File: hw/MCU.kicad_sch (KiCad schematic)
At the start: 18 parts, among them J2 Conn_01x06, SW2 SKRPACE010, SW3 SKRPACE010, U2 N32L406RBL7, Y2 XL2EL89COI-111YLC-8M

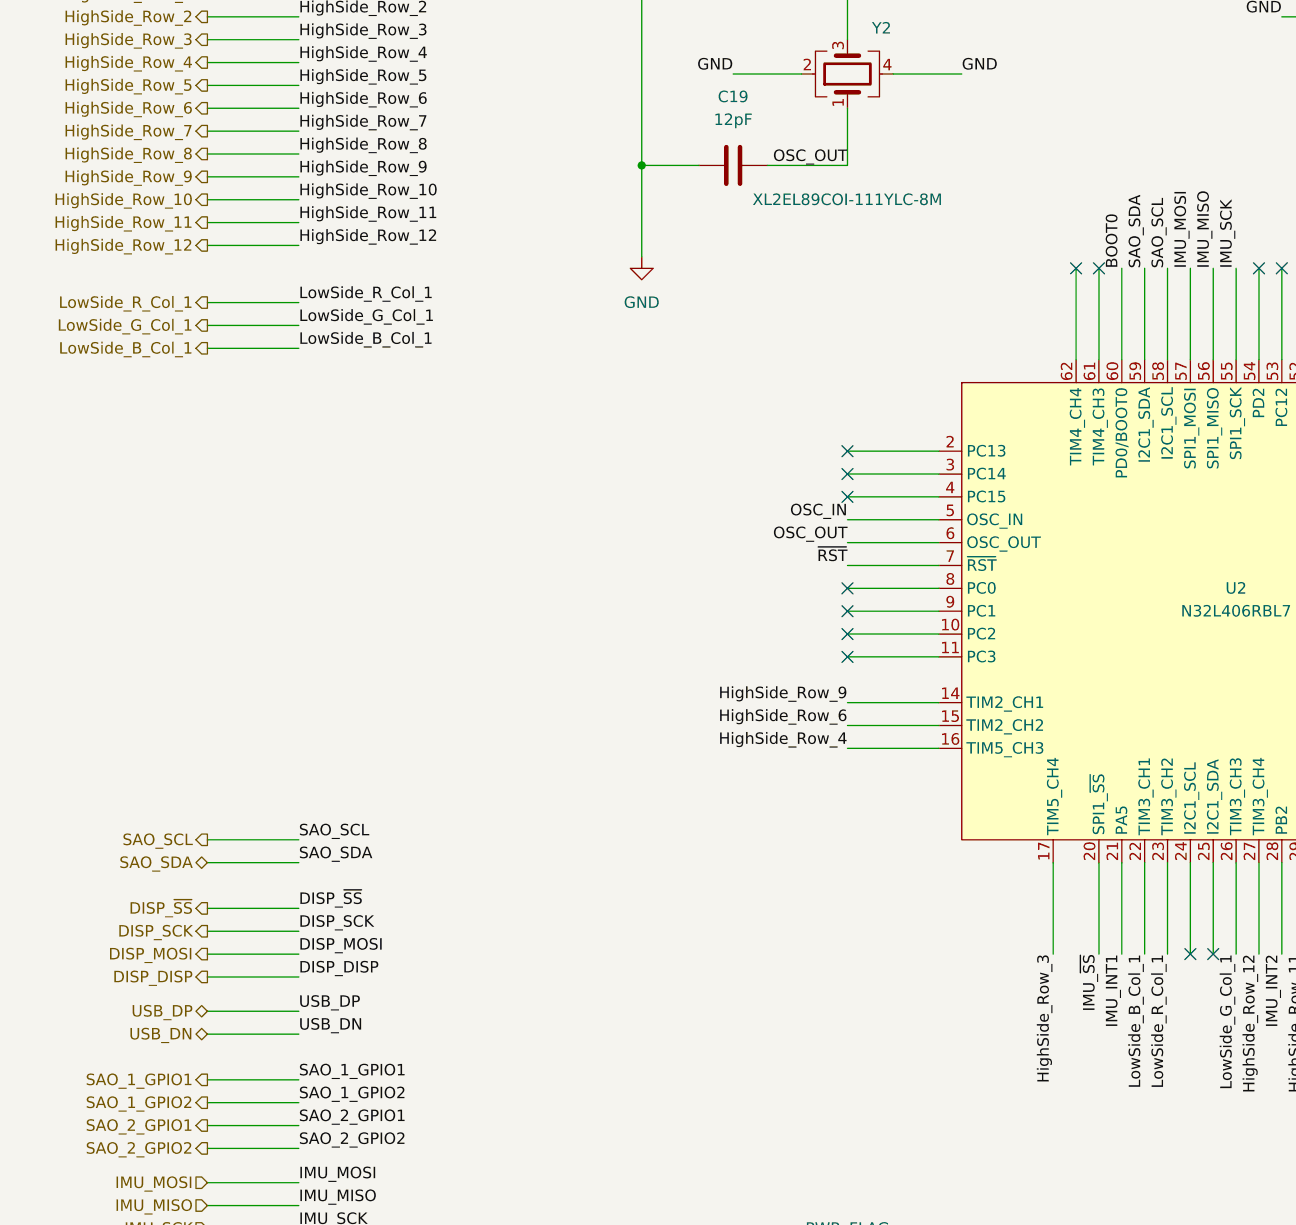
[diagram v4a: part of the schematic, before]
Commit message: added a UART connector
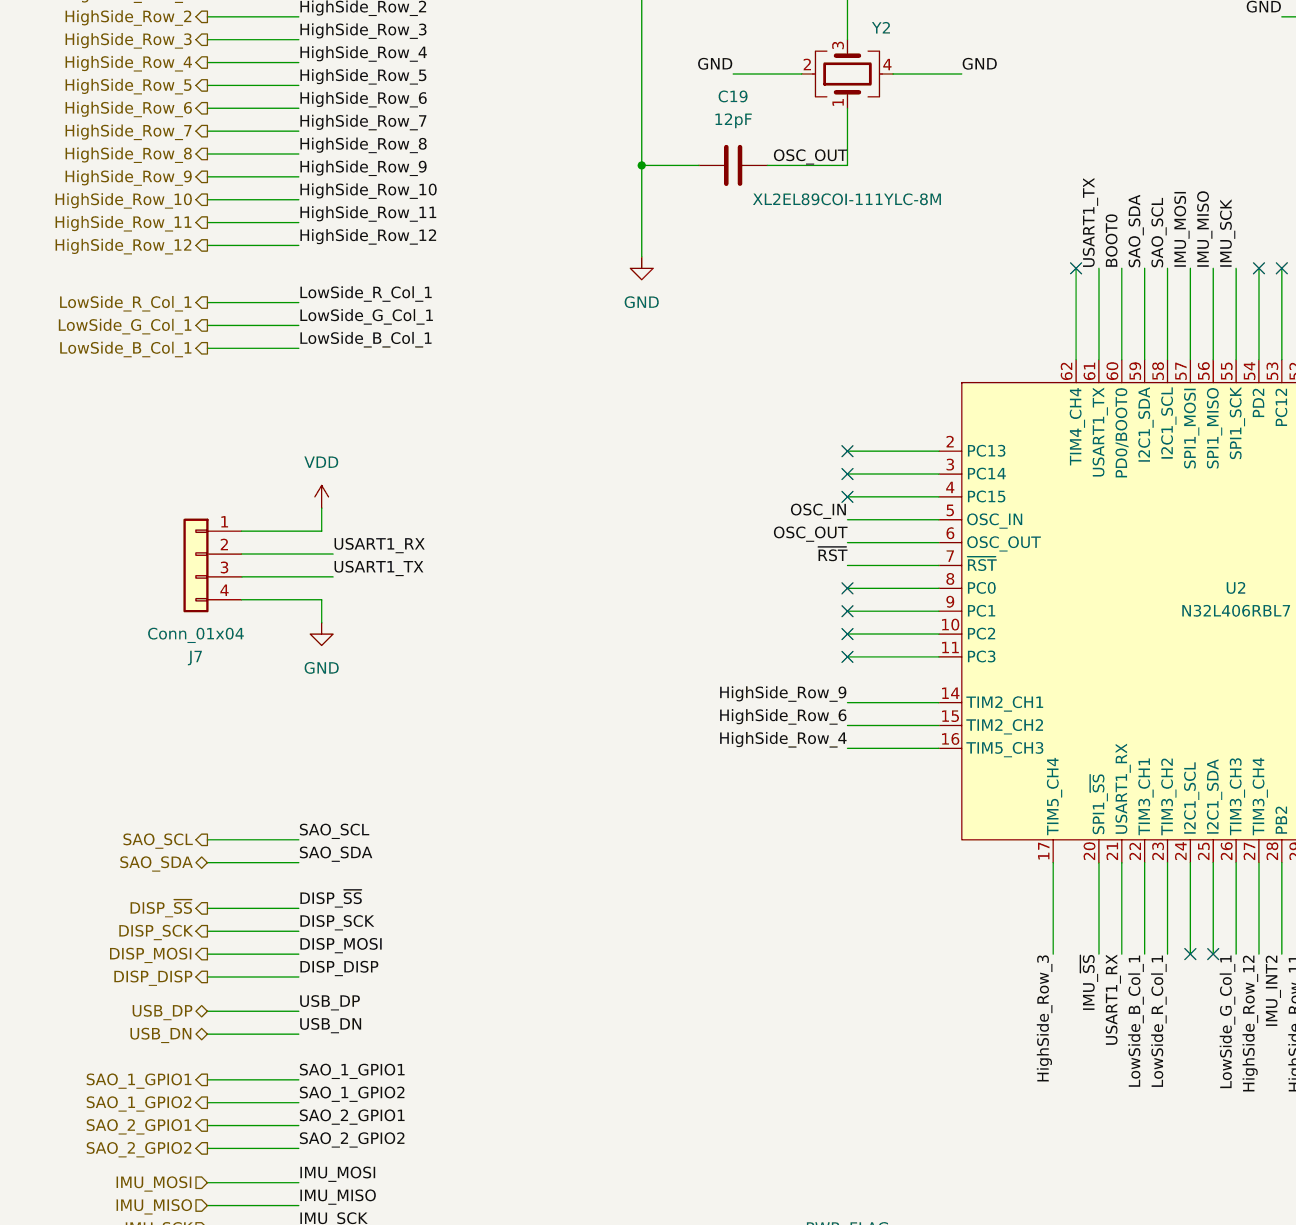
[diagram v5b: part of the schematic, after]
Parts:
- added J7: Conn_01x04, Connector_PinHeader_2.54mm:PinHeader_1x04_P2.54mm_Vertical, symbol Connector_Generic:Conn_01x04
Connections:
- net GND: now also J7.4 (Pin_4)
- net IMU_INT1: no longer U2.21 (PA5)
- net VDD: now also J7.1 (Pin_1)
- net USART1_TX: now reaches U2.61 (PB8)
- net USART1_TX: now also J7.3 (Pin_3)
- new net USART1_RX: J7.2 (Pin_2), U2.21 (PA5)
- no-connect marks 16 -> 15
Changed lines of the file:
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@@
   (junction (at 254 104.14) (diameter 0) (color 0 0 0 0)
   )
-  (no_connect (at 142.24 60.96))
   (no_connect (at 114.3 101.6))
   (no_connect (at 182.88 127))
@@
     (stroke (width 0) (type default))
   )
+  (wire (pts (xy 55.88 90.17) (xy 46.99 90.17))
+    (stroke (width 0) (type default))
+  )
   (wire (pts (xy 261.62 33.02) (xy 274.32 33.02))
     (stroke (width 0) (type default))
@@
     (stroke (width 0) (type default))
   )
+  (wire (pts (xy 55.88 87.63) (xy 55.88 90.17))
+    (stroke (width 0) (type default))
+  )
   (wire (pts (xy 43.18 167.64) (xy 53.34 167.64))
     (stroke (width 0) (type default))
@@
     (stroke (width 0) (type default))
   )
+  (wire (pts (xy 46.99 95.25) (xy 57.15 95.25))
+    (stroke (width 0) (type default))
+  )
   (wire (pts (xy 40.64 21.59) (xy 40.64 25.4))
     (stroke (width 0) (type default))
@@
     (stroke (width 0) (type default))
   )
+  (wire (pts (xy 46.99 97.79) (xy 55.88 97.79))
+    (stroke (width 0) (type default))
+  )
   (wire (pts (xy 162.56 71.12) (xy 162.56 60.96))
     (stroke (width 0) (type default))
@@
     (stroke (width 0) (type default))
   )
+  (wire (pts (xy 46.99 92.71) (xy 57.15 92.71))
+    (stroke (width 0) (type default))
+  )
   (wire (pts (xy 124.46 99.06) (xy 114.3 99.06))
     (stroke (width 0) (type default))
@@
     (stroke (width 0) (type default))
   )
+  (wire (pts (xy 55.88 97.79) (xy 55.88 100.33))
+    (stroke (width 0) (type default))
+  )
   (wire (pts (xy 168.91 20.32) (xy 162.56 20.32))
     (stroke (width 0) (type default))
@@
     (effects (font (size 1.27 1.27)) (justify left bottom))
   )
+  (label "USART1_TX" (at 57.15 95.25 0) (fields_autoplaced)
+    (effects (font (size 1.27 1.27)) (justify left bottom))
+  )
   (label "HighSide_Row_4" (at 53.34 38.1 0) (fields_autoplaced)
     (effects (font (size 1.27 1.27)) (justify left bottom))
@@
     (effects (font (size 1.27 1.27)) (justify right bottom))
   )
-  (label "IMU_INT1" (at 144.78 137.16 270) (fields_autoplaced)
+  (label "USART1_RX" (at 144.78 137.16 270) (fields_autoplaced)
     (effects (font (size 1.27 1.27)) (justify right bottom))
   )
@@
     (effects (font (size 1.27 1.27)) (justify right bottom))
   )
+  (label "USART1_TX" (at 142.24 60.96 90) (fields_autoplaced)
+    (effects (font (size 1.27 1.27)) (justify left bottom))
+  )
   (label "LowSide_R_Col_1" (at 53.34 64.77 0) (fields_autoplaced)
     (effects (font (size 1.27 1.27)) (justify left bottom))
@@
     (effects (font (size 1.27 1.27)) (justify left bottom))
   )
+  (label "USART1_RX" (at 57.15 92.71 0) (fields_autoplaced)
+    (effects (font (size 1.27 1.27)) (justify left bottom))
+  )
   (label "OSC_OUT" (at 114.3 49.53 180) (fields_autoplaced)
     (effects (font (size 1.27 1.27)) (justify right bottom))
@@
     )
   )
+  (symbol (lib_id "power:GND") (at 55.88 100.33 0) (unit 1)
+    (in_bom yes) (on_board yes) (dnp no) (fields_autoplaced)
+    (property "Reference" "#PWR023" (at 55.88 106.68 0)
+      (effects (font (size 1.27 1.27)) hide)
+    )
+    (property "Value" "GND" (at 55.88 105.41 0)
+      (effects (font (size 1.27 1.27)))
+    )
+    (property "Footprint" "" (at 55.88 100.33 0)
+      (effects (font (size 1.27 1.27)) hide)
+    )
+    (property "Datasheet" "" (at 55.88 100.33 0)
+      (effects (font (size 1.27 1.27)) hide)
+    )
+    (pin "1")
+    (instances
+      (project "KiConSZ2023"
+        (path "/8659c260-f029-4e72-8b9a-85fff45eea40/aebeadc6-0cb2-44f8-88a5-80ae76b1b2bc"
+          (reference "#PWR023") (unit 1)
+        )
+      )
+    )
+  )
   (symbol (lib_id "power:VDDA") (at 63.5 21.59 0) (unit 1)
     (in_bom yes) (on_board yes) (dnp no) (fields_autoplaced)
@@
     (pin "2")
     (pin "20" (alternate "SPI1_~{SS}"))
-    (pin "21")
+    (pin "21" (alternate "USART1_RX"))
     (pin "22" (alternate "TIM3_CH1"))
     (pin "23" (alternate "TIM3_CH2"))
@@
     (pin "6" (alternate "OSC_OUT"))
     (pin "60")
-    (pin "61" (alternate "TIM4_CH3"))
+    (pin "61" (alternate "USART1_TX"))
     (pin "62" (alternate "TIM4_CH4"))
     (pin "63")
@@
     )
   )
+  (symbol (lib_id "power:VDD") (at 55.88 87.63 0) (unit 1)
+    (in_bom yes) (on_board yes) (dnp no) (fields_autoplaced)
+    (property "Reference" "#PWR022" (at 55.88 91.44 0)
+      (effects (font (size 1.27 1.27)) hide)
+    )
+    (property "Value" "VDD" (at 55.88 82.55 0)
+      (effects (font (size 1.27 1.27)))
+    )
+    (property "Footprint" "" (at 55.88 87.63 0)
+      (effects (font (size 1.27 1.27)) hide)
+    )
+    (property "Datasheet" "" (at 55.88 87.63 0)
+      (effects (font (size 1.27 1.27)) hide)
+    )
+    (pin "1")
+    (instances
+      (project "KiConSZ2023"
+        (path "/8659c260-f029-4e72-8b9a-85fff45eea40/aebeadc6-0cb2-44f8-88a5-80ae76b1b2bc"
+          (reference "#PWR022") (unit 1)
+        )
+      )
+    )
+  )
   (symbol (lib_id "Device:C") (at 101.6 27.94 90) (unit 1)
     (in_bom yes) (on_board yes) (dnp no) (fields_autoplaced)
@@
         )
       )
+    )
+  )
+  (symbol (lib_id "Connector_Generic:Conn_01x04") (at 41.91 92.71 0) (mirror y) (unit 1)
+    (in_bom yes) (on_board yes) (dnp no)
+    (property "Reference" "J7" (at 41.91 104.14 0)
+      (effects (font (size 1.27 1.27)))
+    )
+    (property "Value" "Conn_01x04" (at 41.91 101.6 0)
+      (effects (font (size 1.27 1.27)))
+    )
+    (property "Footprint" "Connector_PinHeader_2.54mm:PinHeader_1x04_P2.54mm_Vertical" (at 41.91 92.71 0)
+      (effects (font (size 1.27 1.27)) hide)
+    )
+    (property "Datasheet" "~" (at 41.91 92.71 0)
+      (effects (font (size 1.27 1.27)) hide)
+    )
+    (pin "1")
+    (pin "2")
+    (pin "3")
+    (pin "4")
+    (instances
+      (project "KiConSZ2023"
+        (path "/8659c260-f029-4e72-8b9a-85fff45eea40/aebeadc6-0cb2-44f8-88a5-80ae76b1b2bc"
+          (reference "J7") (unit 1)
+        )
+      )

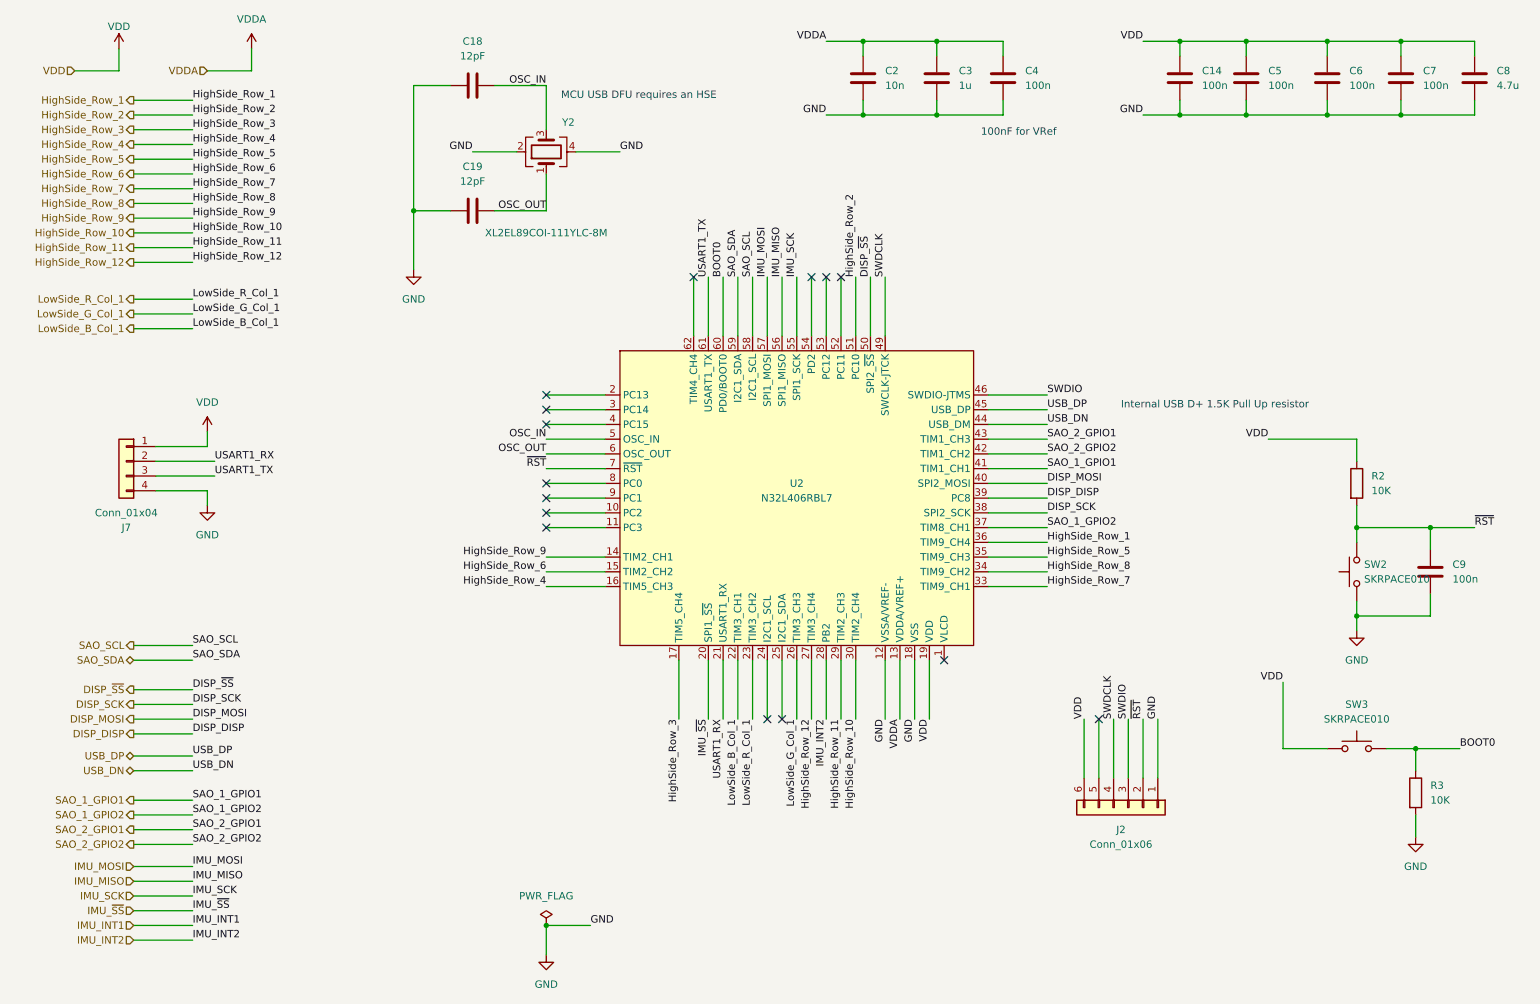
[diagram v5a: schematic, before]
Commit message: revert Display connector
fix SPI SS naming
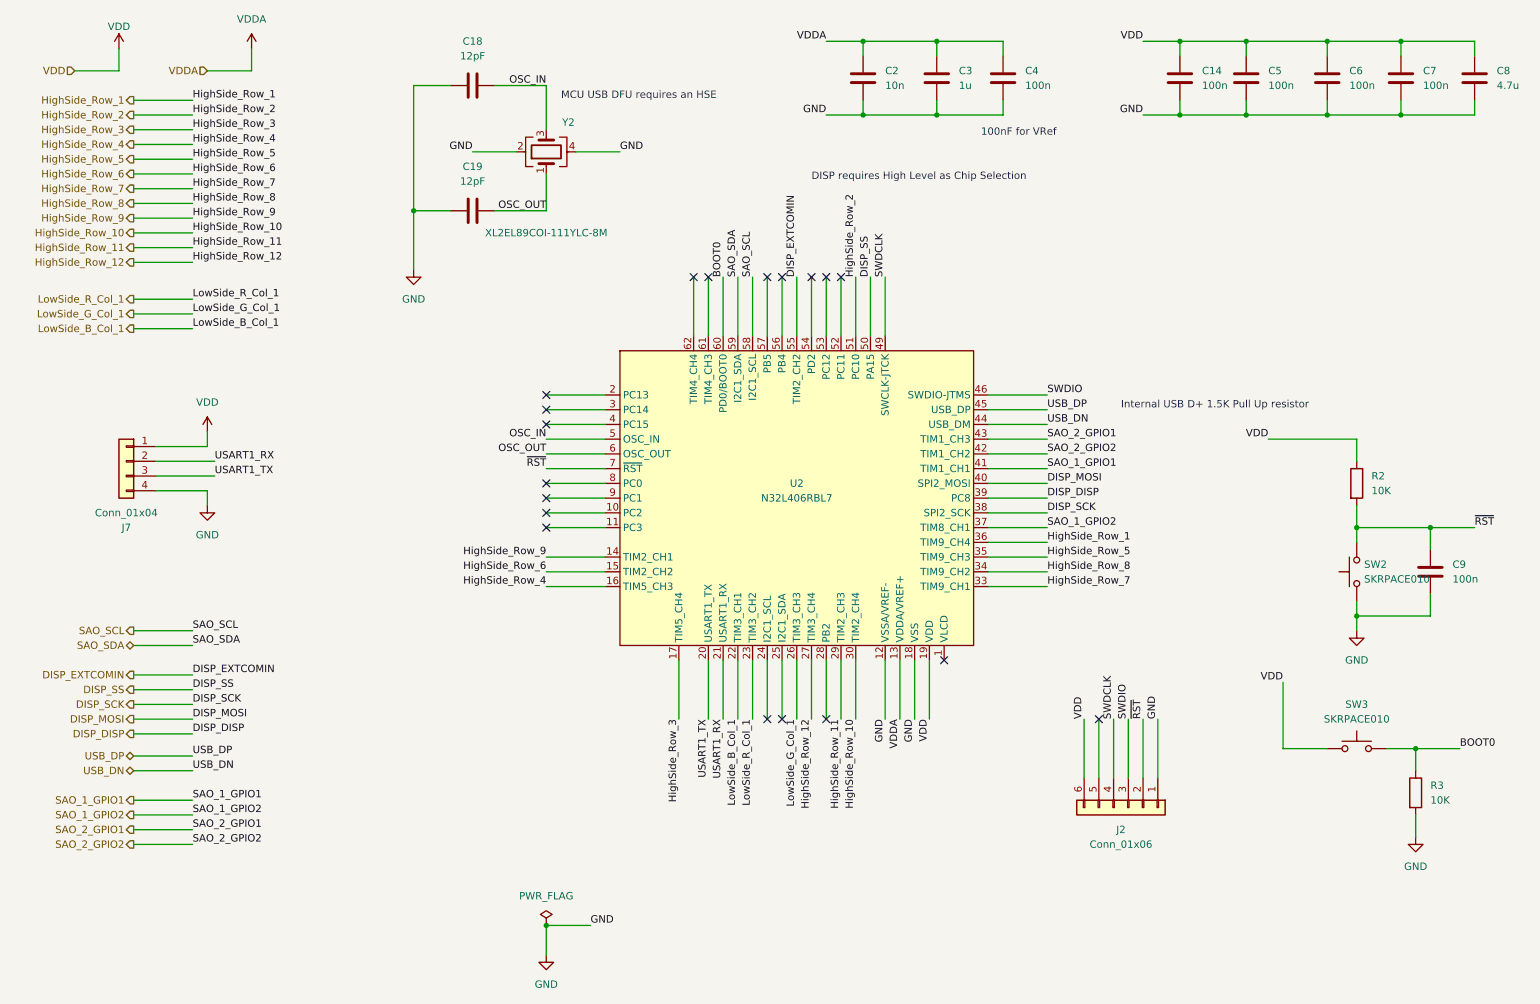
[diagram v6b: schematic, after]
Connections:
- net IMU_~{SS} is gone; now on net USART1_TX: U2.20 (PA4)
- net USART1_TX: no longer U2.61 (PB8)
- net DISP_~{SS} renamed DISP_SS
- net IMU_INT2: no longer names the net of U2.28 (PB2)
- net IMU_MISO: no longer names the net of U2.56 (PB4)
- net IMU_MOSI: no longer names the net of U2.57 (PB5)
- net IMU_SCK renamed DISP_EXTCOMIN
- no-connect marks 15 -> 19
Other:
- note added: "DISP requires High Level as Chip Selection"
